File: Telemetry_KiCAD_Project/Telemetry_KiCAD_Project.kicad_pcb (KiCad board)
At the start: 4 copper layers, 80 x 87.3 mm, 62 parts, among them J1 50Ω SMA Connector, J2 DB37_Male, J3 10118192-0001LF, U1 RSD-897.500-942.500-1612-TR, U2 Si4463, U3 ADL5521, U4 Si4463, U5 STM32L562VET, U6 LM317T, U7 USBLC6-2SC6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

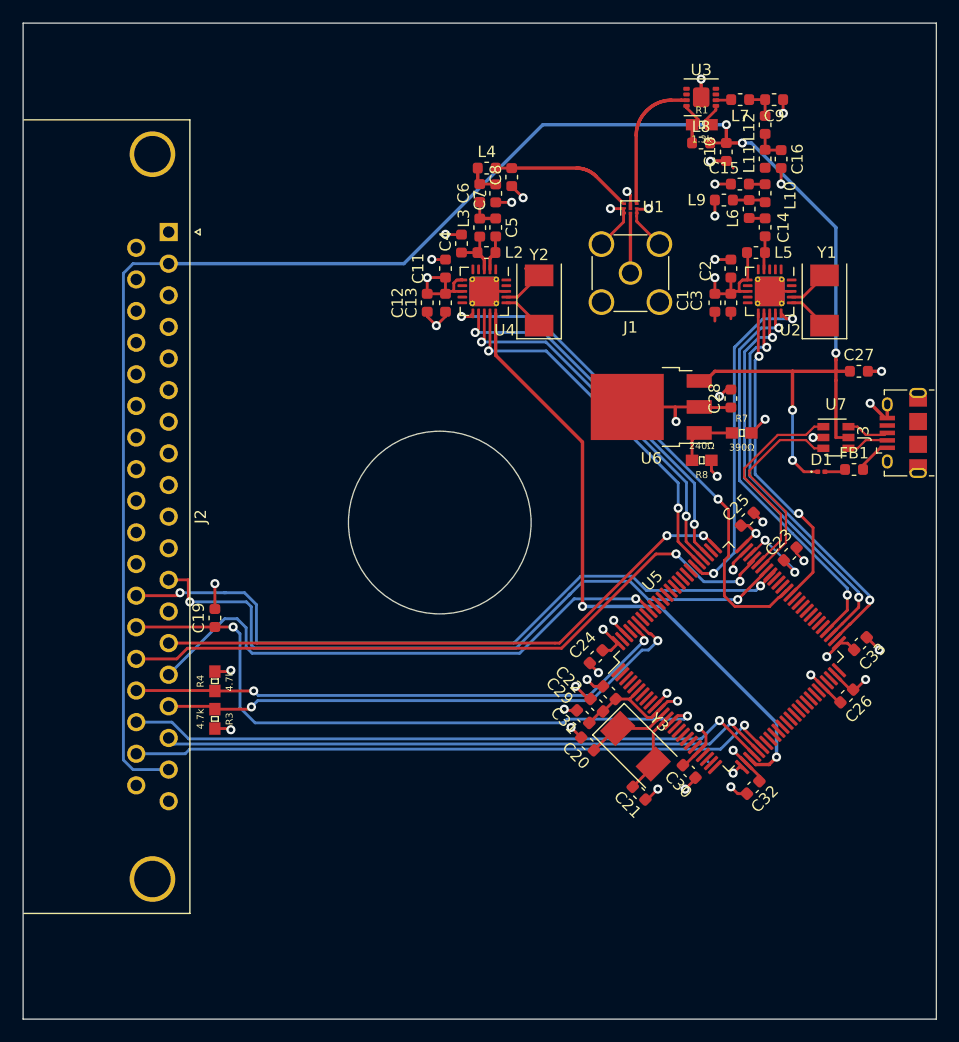
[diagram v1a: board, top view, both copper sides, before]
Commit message: Added via fences to RF section, adjusted labels
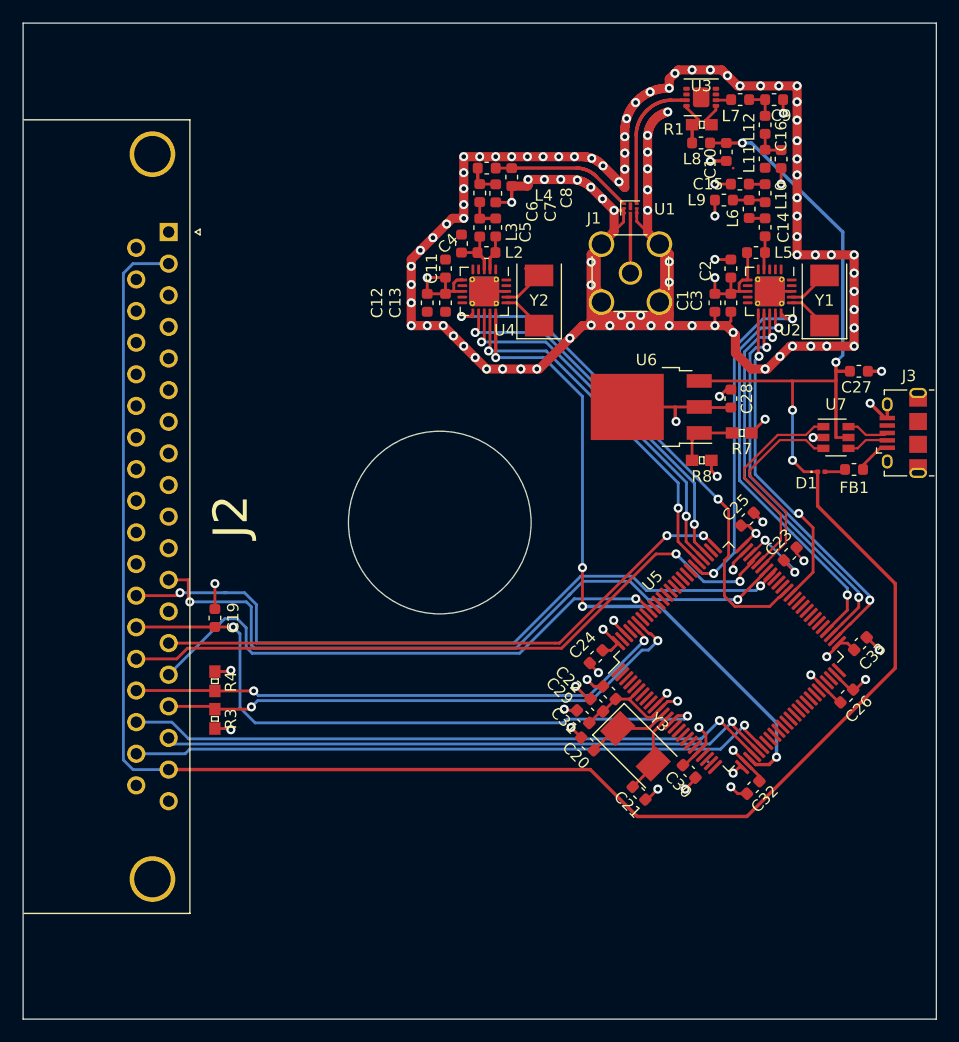
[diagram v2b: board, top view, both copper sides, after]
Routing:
- net GND: track 70.6 -> 261.4 mm, vias 36 -> 125
- net +5V: track 164.3 -> 199.8 mm, vias 5 -> 4
- net /~RX_SEL: track 55.8 -> 58.1 mm, vias 2 -> 4
- net (no net): track 7.10 -> 6.23 mm, vias 1 -> 0

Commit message: Added RDT logo and edge graphics
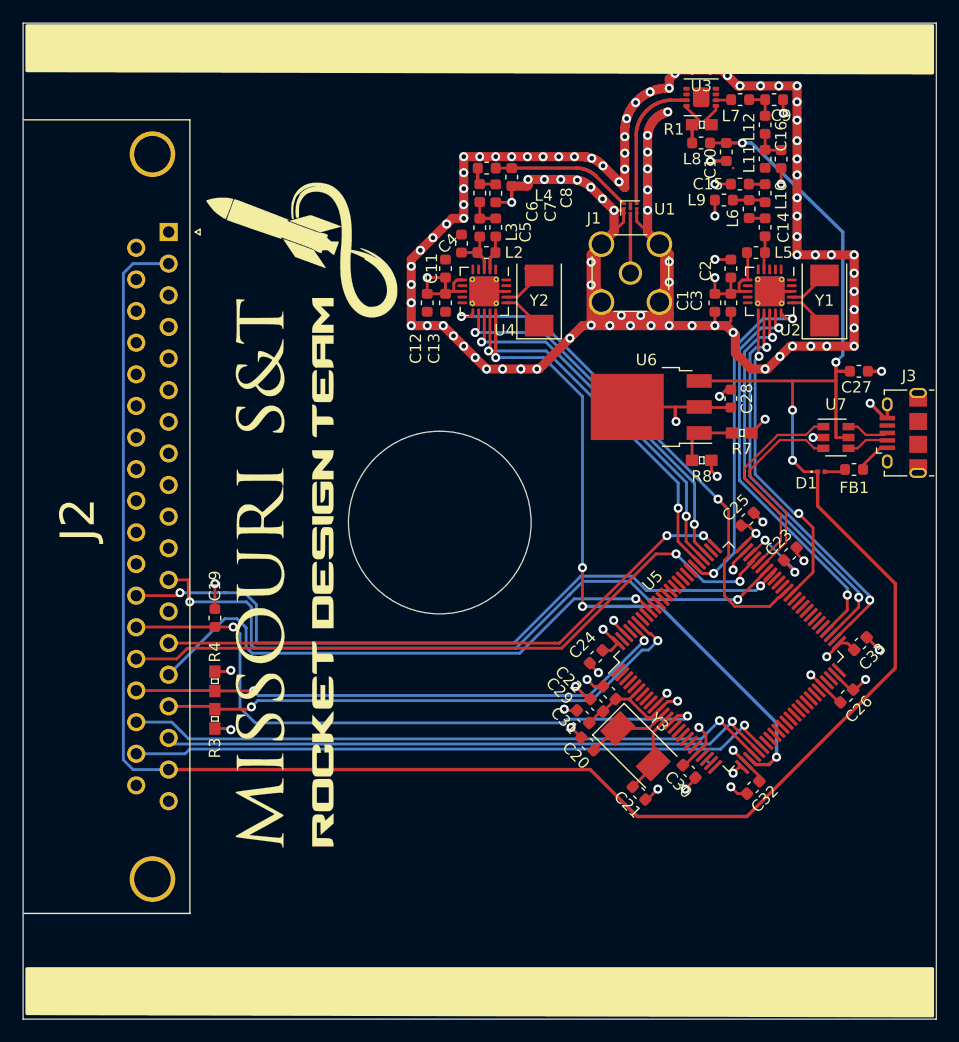
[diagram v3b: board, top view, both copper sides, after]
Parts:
- added G***: LOGO, Custom_Graphics:RDT_Logo, F.Cu at (131.2, 98.4)

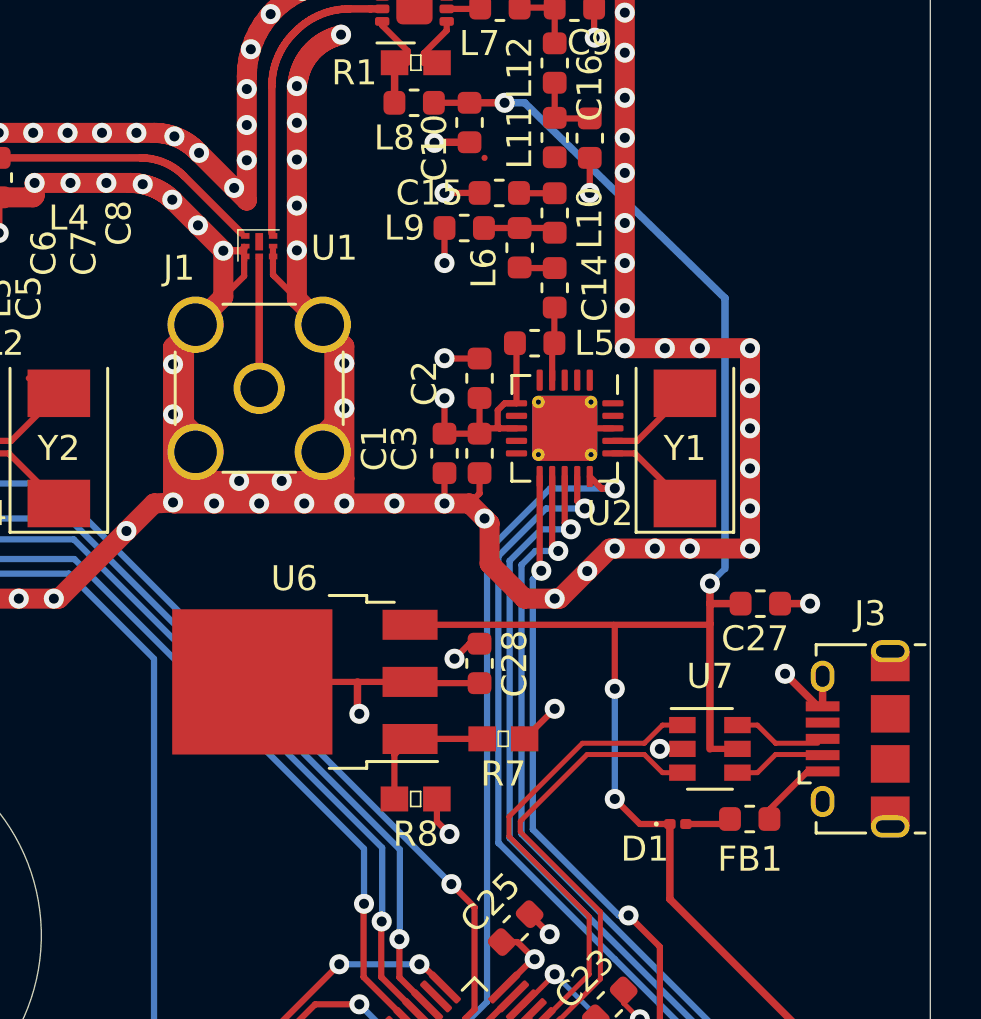
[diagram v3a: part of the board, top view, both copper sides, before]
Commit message: Fixed unconnected ground pin on duplexer chip
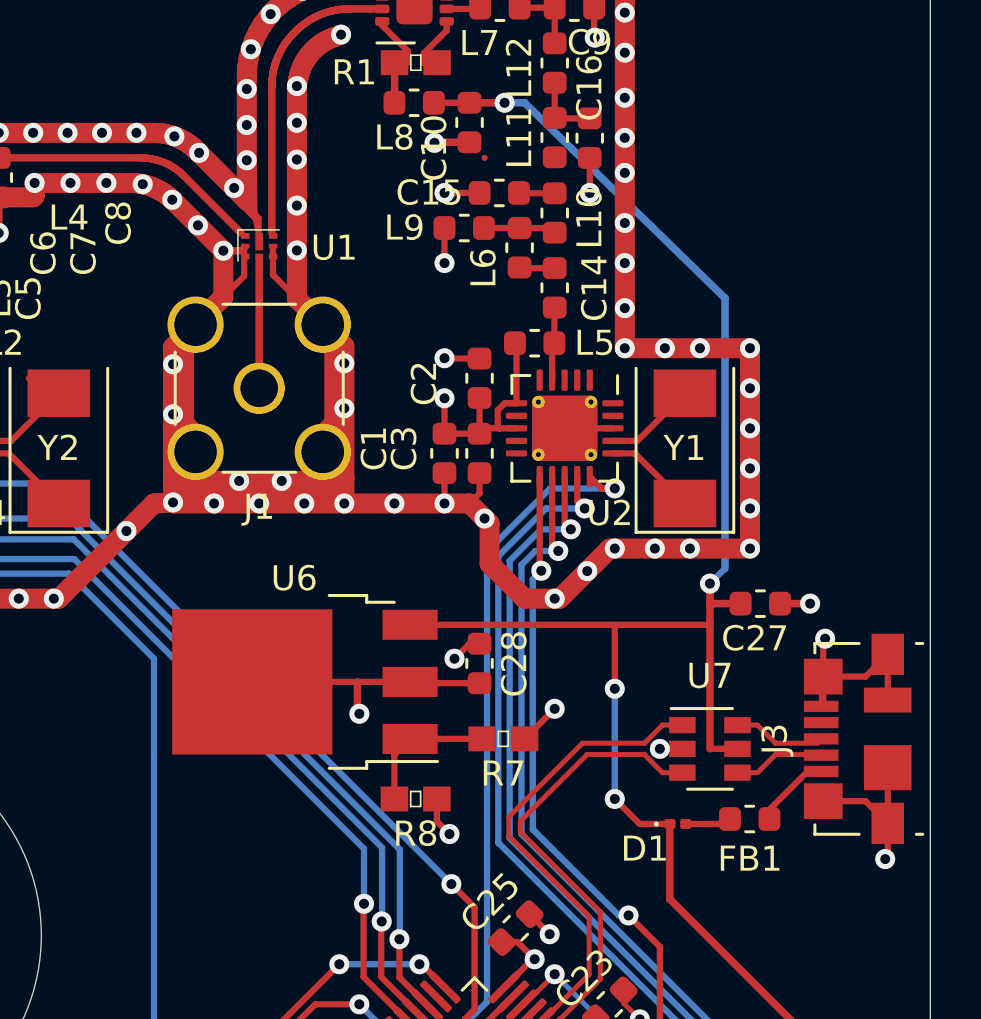
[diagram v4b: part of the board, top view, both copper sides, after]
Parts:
- J3: footprint Connector_USB:USB_Micro-B_Amphenol_10118194_Horizontal -> Connector_USB:USB_Micro-B_Molex_47346-0001
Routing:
- net GND: track 261.4 -> 272.3 mm
- net (no net): track 6.23 -> 6.63 mm, vias 0 -> 1

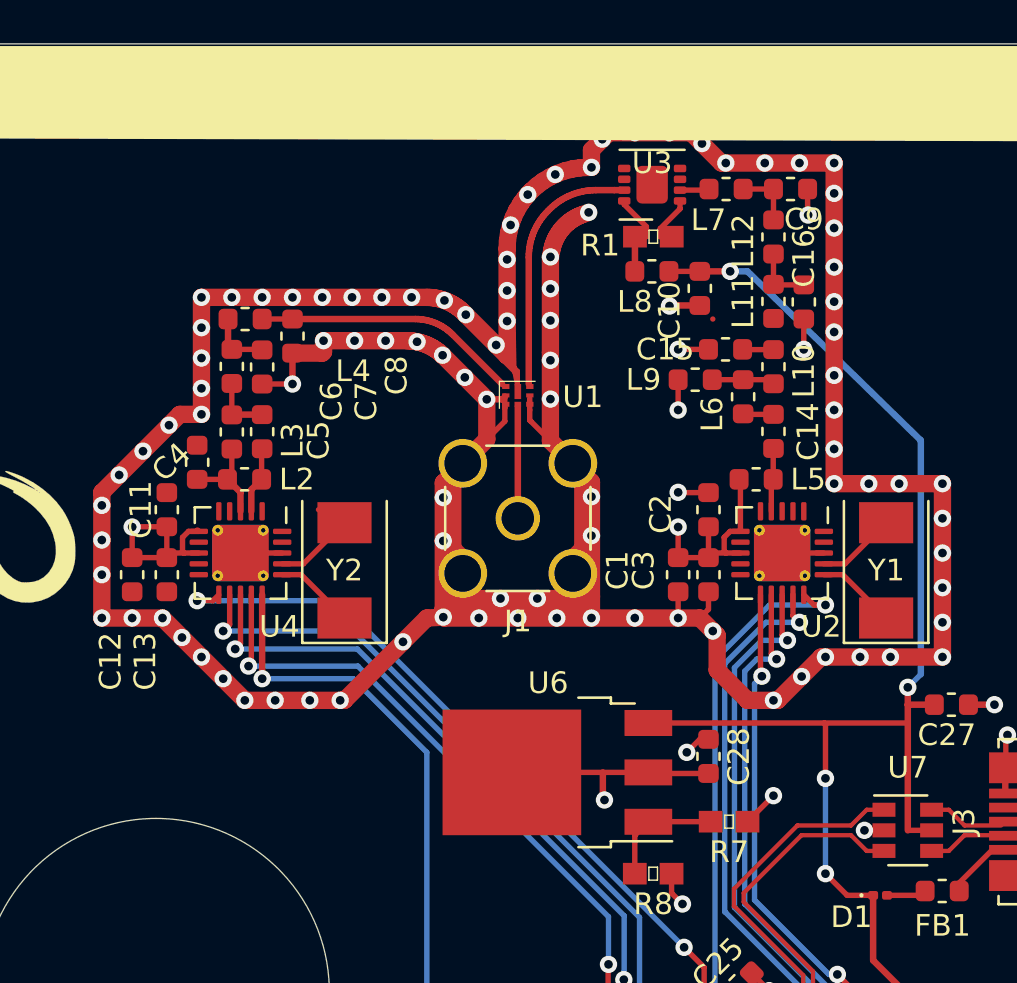
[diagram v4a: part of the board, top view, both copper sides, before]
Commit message: Fixed more unconnected ground pads
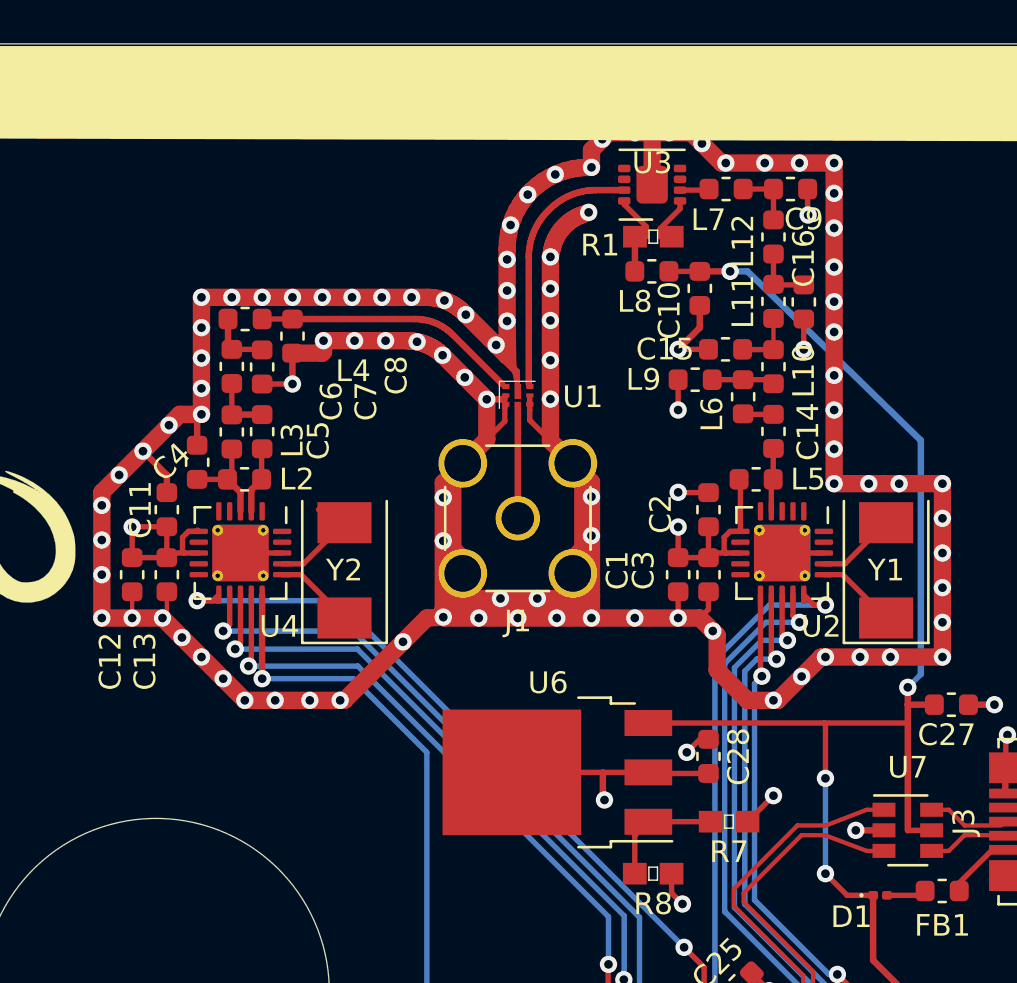
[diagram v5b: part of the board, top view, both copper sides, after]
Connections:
- J3 pad 6: (no net) -> GND
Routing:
- net GND: track 272.3 -> 289.2 mm
- net (no net): track 6.63 -> 0.00 mm, vias 1 -> 0
- net Net-(C15-Pad1): track 1.45 -> 2.89 mm
